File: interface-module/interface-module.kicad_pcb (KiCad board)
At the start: 2 copper layers, 79 x 83 mm, 117 parts, among them J1 Conn_01x08, J2 Conn_01x08, J3 Conn_01x02, Q201 PMOS, Q202 NMOS, Q203 PMOS, Q204 NMOS, Q205 PMOS, Q206 NMOS, Q207 PMOS, Q208 NMOS, Q209 PMOS, Q210 NMOS, Q211 PMOS, Q212 NMOS, Q213 PMOS, Q214 NMOS, Q215 PMOS, Q216 NMOS, SW1 SW_Coded_SH-7050, U101 MCP3464, U201 140357145200, U202 140357145200, U203 140357145200, U204 140357145200, U205 140357145200, U206 140357145200, U207 140357145200, U208 140357145200, U301 TCA9548

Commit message: Added address pin labels
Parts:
- R2: value CFG1 -> INFO1
- R4: value CFG2 -> INFO2
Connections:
- net Net-(U1-PA4) renamed /ADDR_4
- net Net-(U1-PA5) renamed /ADDR_1
- net Net-(U1-PA6) renamed /ADDR_8
- net Net-(U1-PA7) renamed /ADDR_2

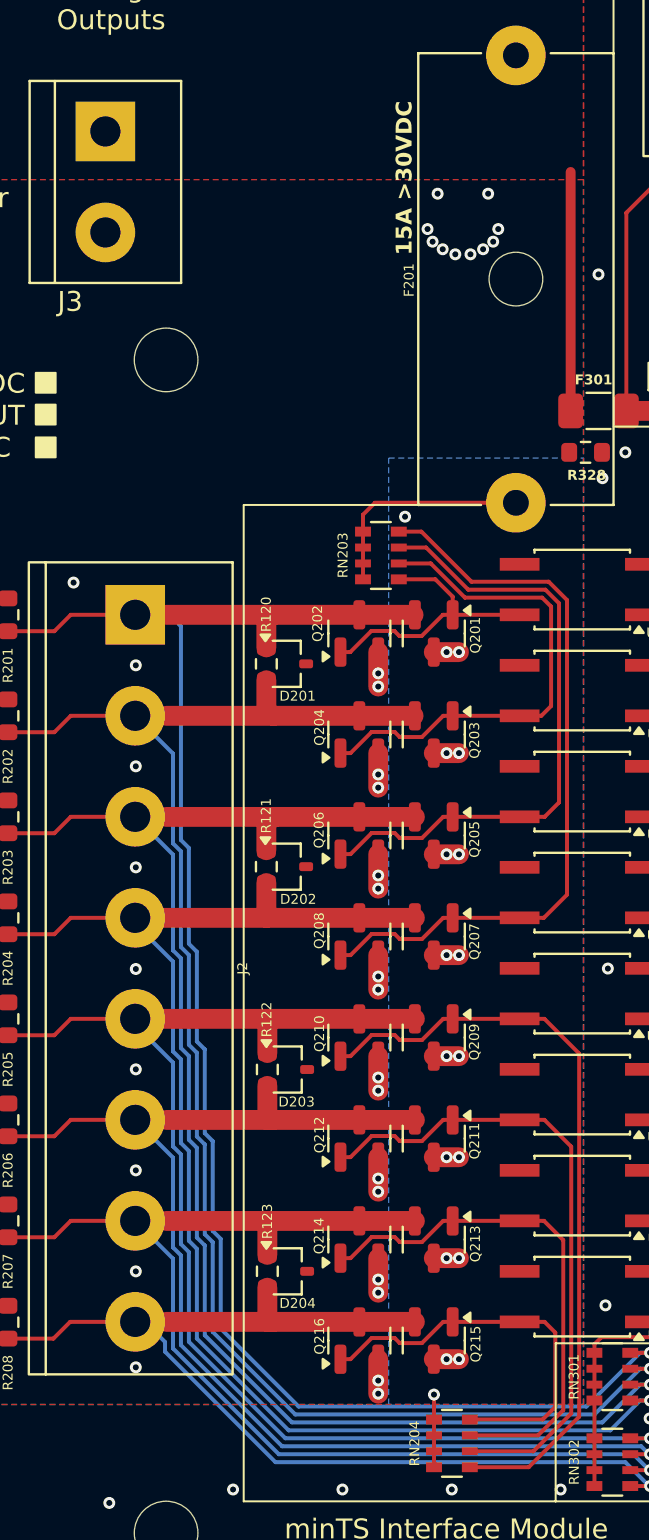
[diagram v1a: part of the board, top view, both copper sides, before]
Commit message: Revision, updated diodes and transistors
Moved to a more robust transistor arrangement with a new zener diode
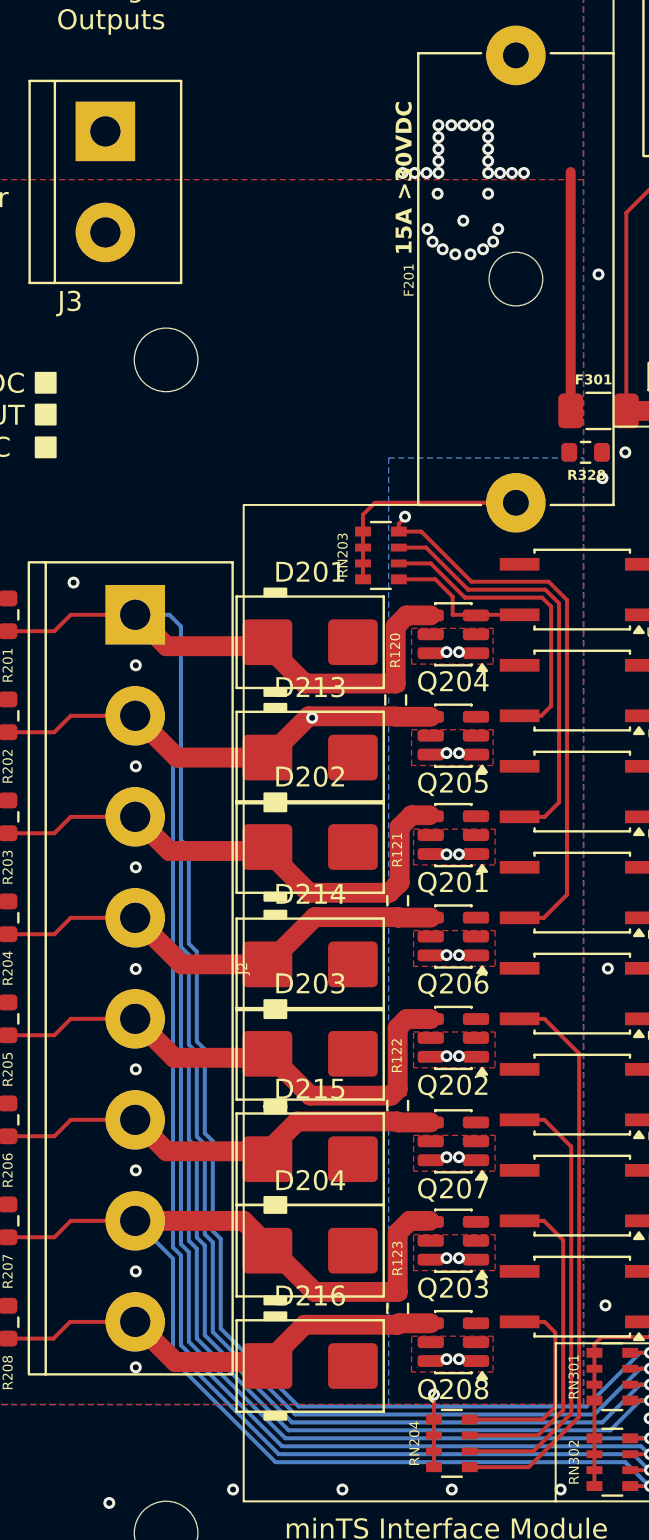
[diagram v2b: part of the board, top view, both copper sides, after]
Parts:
- removed Q209, Q211, Q213, Q215: PMOS, Package_TO_SOT_SMD:SOT-23
- removed Q210, Q212, Q214, Q216: NMOS, Package_TO_SOT_SMD:SOT-23
- added D213: SMBJ5.0A, PCM_Diode_SMD_AKL:D_SMB, F.Cu at (121.8, 103.7)
- added D214: SMBJ5.0A, PCM_Diode_SMD_AKL:D_SMB, F.Cu at (121.8, 114.1)
- added D215: SMBJ5.0A, PCM_Diode_SMD_AKL:D_SMB, F.Cu at (121.8, 123.9)
- added D216: SMBJ5.0A, PCM_Diode_SMD_AKL:D_SMB, F.Cu at (121.8, 134.3)
- D201, D202, D203, D204: value MMBD717LT1G -> SMBJ5.0A; footprint Package_TO_SOT_SMD:SOT-323_SC-70 -> PCM_Diode_SMD_AKL:D_SMB
- Q201, Q203, Q205, Q207: value PMOS -> DMP3050LVT-7; footprint Package_TO_SOT_SMD:SOT-23 -> Package_TO_SOT_SMD:TSOT-23-6
- Q202, Q204, Q206, Q208: value NMOS -> DMP3050LVT-7; footprint Package_TO_SOT_SMD:SOT-23 -> Package_TO_SOT_SMD:TSOT-23-6
- moved Q203 25.5 mm to (129.0, 128.0), turned to 180 degrees
- moved Q208 20.9 mm to (129.0, 133.1), turned to 180 degrees
- moved Q202 20.9 mm to (129.0, 117.8), turned to 180 degrees
- moved Q207 10.3 mm to (129.0, 123.0), turned to 180 degrees
- moved Q201 10.2 mm to (129.0, 107.6), turned to 180 degrees
- moved Q206 6.94 mm to (129.0, 112.7), turned to 180 degrees
- moved Q204 6.91 mm to (129.0, 97.5), turned to 180 degrees
- moved R121 6.82 mm to (126.2, 110.9)
- moved R123 6.81 mm to (126.2, 131.4)
- moved R122 6.80 mm to (126.2, 121.2)
- moved R120 6.75 mm to (126.1, 100.8)
- moved Q205 5.12 mm to (129.0, 102.6), turned to 180 degrees
- moved D201 1.62 mm to (121.8, 97.9)
- moved D202 1.56 mm to (121.8, 108.2)
- moved D204 1.55 mm to (121.8, 128.5)
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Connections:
- D201 pad 2: OUT1/IN0- -> AUX_POW-
- D202 pad 2: OUT3/IN1- -> AUX_POW-
- D203 pad 2: OUT5/IN2- -> AUX_POW-
- D204 pad 2: OUT7/IN3- -> AUX_POW-
- Q201 pad 1: /outputs/~{ISO_OUT_0} -> VPOW
- Q201 pad 2: OUT0/IN0+ -> VPOW
- Q201 pad 3: VPOW -> AUX_POW-
- Q202 pad 1: /outputs/~{ISO_OUT_0} -> VPOW
- Q202 pad 2: AUX_POW- -> VPOW
- Q202 pad 3: OUT0/IN0+ -> AUX_POW-
- Q203 pad 1: /outputs/~{ISO_OUT_1} -> VPOW
- Q203 pad 2: OUT1/IN0- -> VPOW
- Q203 pad 3: VPOW -> AUX_POW-
- Q204 pad 1: /outputs/~{ISO_OUT_1} -> VPOW
- Q204 pad 2: AUX_POW- -> VPOW
- Q204 pad 3: OUT1/IN0- -> AUX_POW-
- Q205 pad 1: /outputs/~{ISO_OUT_2} -> VPOW
- Q205 pad 2: OUT2/IN1+ -> VPOW
- Q205 pad 3: VPOW -> AUX_POW-
- Q206 pad 1: /outputs/~{ISO_OUT_2} -> VPOW
- Q206 pad 2: AUX_POW- -> VPOW
- Q206 pad 3: OUT2/IN1+ -> AUX_POW-
- Q207 pad 1: /outputs/~{ISO_OUT_3} -> VPOW
- Q207 pad 2: OUT3/IN1- -> VPOW
- Q207 pad 3: VPOW -> AUX_POW-
- Q208 pad 1: /outputs/~{ISO_OUT_3} -> VPOW
- Q208 pad 2: AUX_POW- -> VPOW
- Q208 pad 3: OUT3/IN1- -> AUX_POW-
- RN203 pad 5: /outputs/~{ISO_OUT_0} -> AUX_POW-
- RN203 pad 6: /outputs/~{ISO_OUT_1} -> AUX_POW-
- RN203 pad 7: /outputs/~{ISO_OUT_2} -> AUX_POW-
- RN203 pad 8: /outputs/~{ISO_OUT_3} -> AUX_POW-
- RN204 pad 5: /outputs/~{ISO_OUT_4} -> AUX_POW-
- RN204 pad 6: /outputs/~{ISO_OUT_5} -> AUX_POW-
- RN204 pad 7: /outputs/~{ISO_OUT_6} -> AUX_POW-
- RN204 pad 8: /outputs/~{ISO_OUT_7} -> AUX_POW-
- U201 pad 4: /outputs/~{ISO_OUT_0} -> AUX_POW-
- U202 pad 4: /outputs/~{ISO_OUT_1} -> AUX_POW-
- U203 pad 4: /outputs/~{ISO_OUT_2} -> AUX_POW-
- U204 pad 4: /outputs/~{ISO_OUT_3} -> AUX_POW-
- U205 pad 4: /outputs/~{ISO_OUT_4} -> AUX_POW-
- U206 pad 4: /outputs/~{ISO_OUT_5} -> AUX_POW-
- U207 pad 4: /outputs/~{ISO_OUT_6} -> AUX_POW-
- U208 pad 4: /outputs/~{ISO_OUT_7} -> AUX_POW-
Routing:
- net AUX_POW-: track 13.9 -> 150.1 mm, vias 36 -> 21
- net /outputs/~{ISO_OUT_4}: track 38.5 -> 0.00 mm
- net /outputs/~{ISO_OUT_3}: track 37.6 -> 0.00 mm
- net /outputs/~{ISO_OUT_5}: track 32.5 -> 0.00 mm
- net /outputs/~{ISO_OUT_2}: track 31.5 -> 0.00 mm
- net /outputs/~{ISO_OUT_6}: track 26.4 -> 0.00 mm
- net /outputs/~{ISO_OUT_1}: track 25.3 -> 0.00 mm
- net /outputs/~{ISO_OUT_7}: track 20.3 -> 0.00 mm
- net /outputs/~{ISO_OUT_0}: track 13.7 -> 0.00 mm
- net VPOW: track 25.0 -> 14.9 mm
- net OUT2/IN1+: track 118.6 -> 124.1 mm
- net OUT6/IN3+: track 87.6 -> 92.9 mm
- net OUT0/IN0+: track 136.0 -> 141.3 mm
- net OUT4/IN2+: track 103.5 -> 107.6 mm
- net OUT1/IN0-: track 129.0 -> 131.4 mm, vias 2 -> 3
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- added copper zone on F.Cu, net VPOW

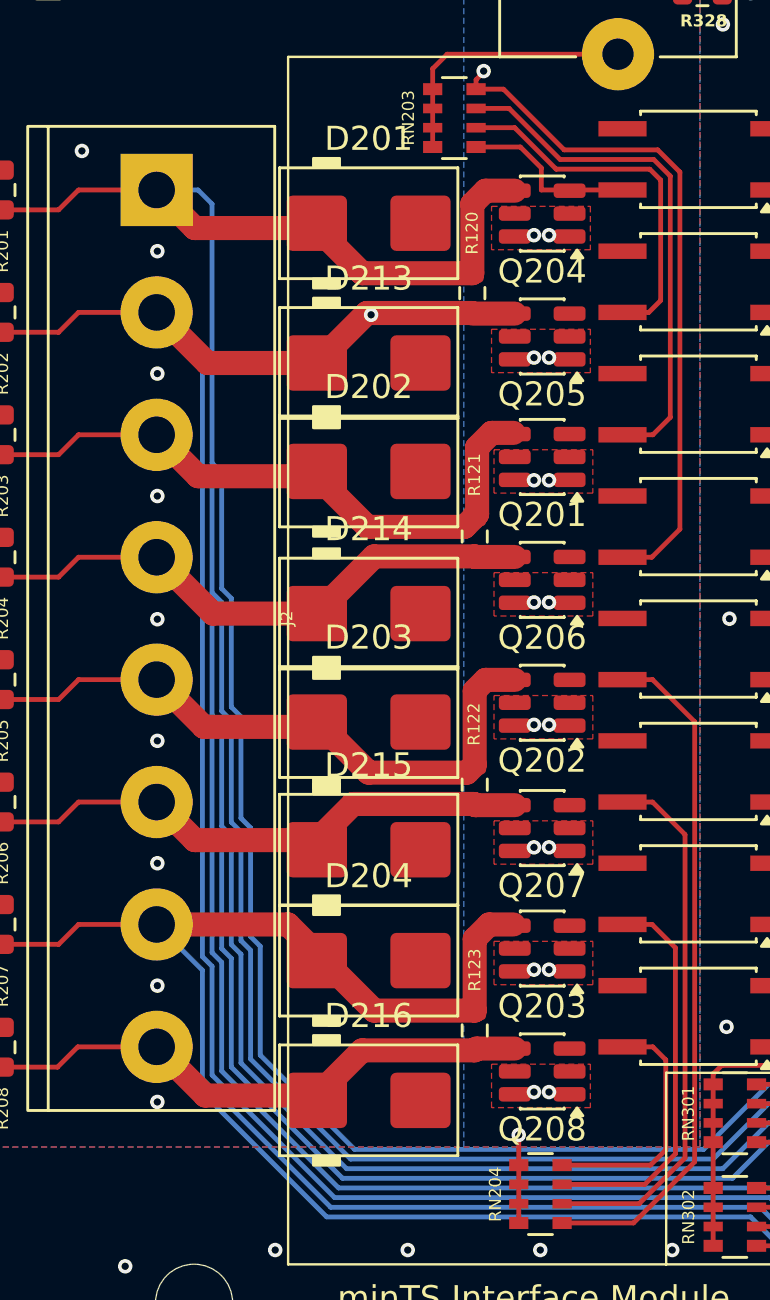
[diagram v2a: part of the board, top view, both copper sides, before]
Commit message: Fixed transistor tracing
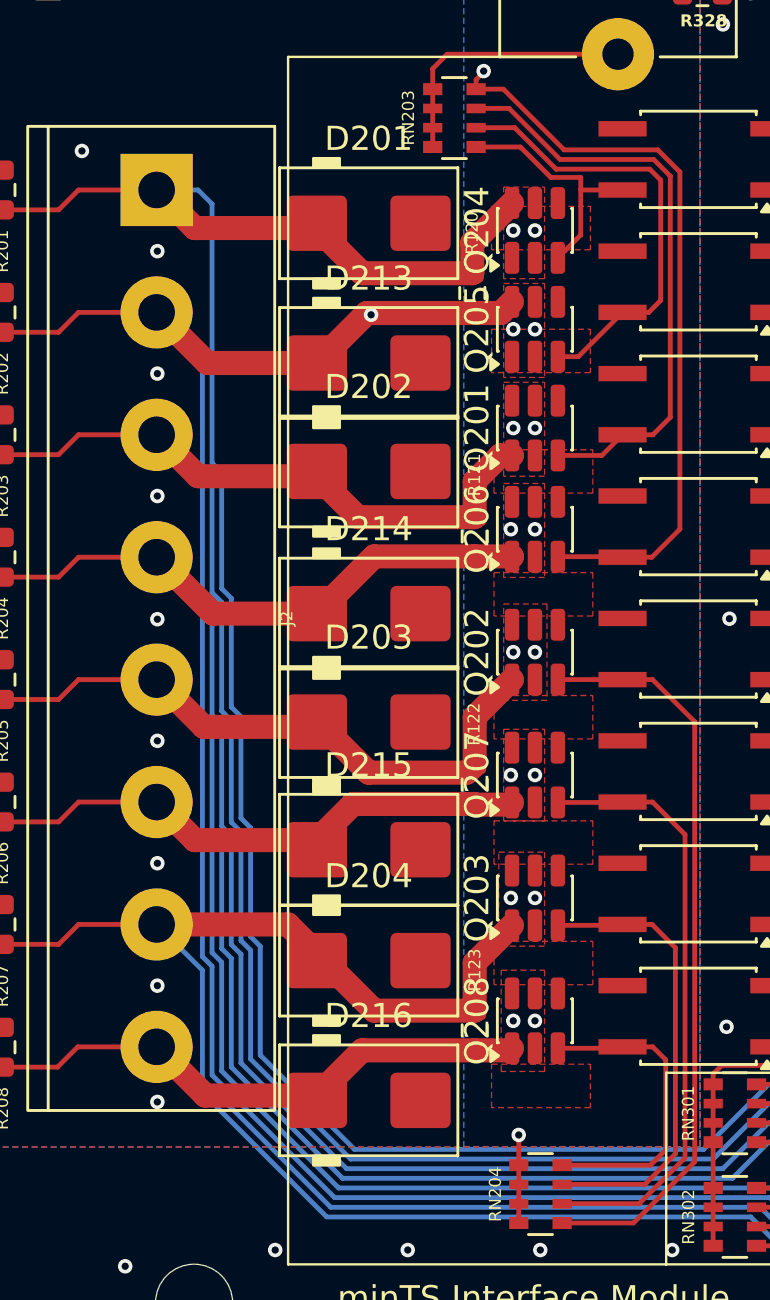
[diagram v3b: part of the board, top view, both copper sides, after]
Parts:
- moved Q207 2.22 mm to (128.7, 120.8), turned to 90 degrees
- moved Q206 2.12 mm to (128.7, 110.6), turned to 90 degrees
- moved Q202 2.12 mm to (128.7, 115.7), turned to 90 degrees
- moved Q203 2.12 mm to (128.7, 125.9), turned to 90 degrees
- moved Q208 2.12 mm to (128.7, 131.0), turned to 90 degrees
- moved Q201 1.24 mm to (128.7, 106.4), turned to 90 degrees
- moved Q204 0.76 mm to (128.7, 98.2), turned to 90 degrees
- moved Q205 0.42 mm to (128.7, 102.3), turned to 90 degrees
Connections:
- Q201 pad 1: VPOW -> OUT2/IN1+
- Q201 pad 2: VPOW -> OUT2/IN1+
- Q201 pad 3: AUX_POW- -> /outputs/~{ISO_OUT_2}
- Q201 pad 4: OUT2/IN1+ -> VPOW
- Q201 pad 5: VPOW -> OUT2/IN1+
- Q201 pad 6: VPOW -> OUT2/IN1+
- Q202 pad 1: VPOW -> OUT4/IN2+
- Q202 pad 2: VPOW -> OUT4/IN2+
- Q202 pad 3: AUX_POW- -> /outputs/~{ISO_OUT_4}
- Q202 pad 4: OUT4/IN2+ -> VPOW
- Q202 pad 5: VPOW -> OUT4/IN2+
- Q202 pad 6: VPOW -> OUT4/IN2+
- Q203 pad 1: VPOW -> OUT6/IN3+
- Q203 pad 2: VPOW -> OUT6/IN3+
- Q203 pad 3: AUX_POW- -> /outputs/~{ISO_OUT_6}
- Q203 pad 4: OUT6/IN3+ -> VPOW
- Q203 pad 5: VPOW -> OUT6/IN3+
- Q203 pad 6: VPOW -> OUT6/IN3+
- Q204 pad 1: VPOW -> OUT0/IN0+
- Q204 pad 2: VPOW -> OUT0/IN0+
- Q204 pad 3: AUX_POW- -> /outputs/~{ISO_OUT_0}
- Q204 pad 4: OUT0/IN0+ -> VPOW
- Q204 pad 5: VPOW -> OUT0/IN0+
- Q204 pad 6: VPOW -> OUT0/IN0+
- Q205 pad 1: VPOW -> OUT1/IN0-
- Q205 pad 2: VPOW -> OUT1/IN0-
- Q205 pad 3: AUX_POW- -> /outputs/~{ISO_OUT_1}
- Q205 pad 4: OUT1/IN0- -> VPOW
- Q205 pad 5: VPOW -> OUT1/IN0-
- Q205 pad 6: VPOW -> OUT1/IN0-
- Q206 pad 1: VPOW -> OUT3/IN1-
- Q206 pad 2: VPOW -> OUT3/IN1-
- Q206 pad 3: AUX_POW- -> /outputs/~{ISO_OUT_3}
- Q206 pad 4: OUT3/IN1- -> VPOW
- Q206 pad 5: VPOW -> OUT3/IN1-
- Q206 pad 6: VPOW -> OUT3/IN1-
- Q207 pad 1: VPOW -> OUT5/IN2-
- Q207 pad 2: VPOW -> OUT5/IN2-
- Q207 pad 3: AUX_POW- -> /outputs/~{ISO_OUT_5}
- Q207 pad 4: OUT5/IN2- -> VPOW
- Q207 pad 5: VPOW -> OUT5/IN2-
- Q207 pad 6: VPOW -> OUT5/IN2-
- Q208 pad 1: VPOW -> OUT7/IN3-
- Q208 pad 2: VPOW -> OUT7/IN3-
- Q208 pad 3: AUX_POW- -> /outputs/~{ISO_OUT_7}
- Q208 pad 4: OUT7/IN3- -> VPOW
- Q208 pad 5: VPOW -> OUT7/IN3-
- Q208 pad 6: VPOW -> OUT7/IN3-
- RN203 pad 5: AUX_POW- -> /outputs/~{ISO_OUT_0}
- RN203 pad 6: AUX_POW- -> /outputs/~{ISO_OUT_1}
- RN203 pad 7: AUX_POW- -> /outputs/~{ISO_OUT_2}
- RN203 pad 8: AUX_POW- -> /outputs/~{ISO_OUT_3}
- RN204 pad 5: AUX_POW- -> /outputs/~{ISO_OUT_4}
- RN204 pad 6: AUX_POW- -> /outputs/~{ISO_OUT_5}
- RN204 pad 7: AUX_POW- -> /outputs/~{ISO_OUT_6}
- RN204 pad 8: AUX_POW- -> /outputs/~{ISO_OUT_7}
- U201 pad 4: AUX_POW- -> /outputs/~{ISO_OUT_0}
- U202 pad 4: AUX_POW- -> /outputs/~{ISO_OUT_1}
- U203 pad 4: AUX_POW- -> /outputs/~{ISO_OUT_2}
- U204 pad 4: AUX_POW- -> /outputs/~{ISO_OUT_3}
- U205 pad 4: AUX_POW- -> /outputs/~{ISO_OUT_4}
- U206 pad 4: AUX_POW- -> /outputs/~{ISO_OUT_5}
- U207 pad 4: AUX_POW- -> /outputs/~{ISO_OUT_6}
- U208 pad 4: AUX_POW- -> /outputs/~{ISO_OUT_7}
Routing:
- net AUX_POW-: track 150.1 -> 0.00 mm
- net /outputs/~{ISO_OUT_4}: track 0.00 -> 31.2 mm
- net /outputs/~{ISO_OUT_3}: track 0.00 -> 31.1 mm
- net /outputs/~{ISO_OUT_5}: track 0.00 -> 25.1 mm
- net /outputs/~{ISO_OUT_2}: track 0.00 -> 24.6 mm
- net /outputs/~{ISO_OUT_6}: track 0.00 -> 19.1 mm
- net /outputs/~{ISO_OUT_1}: track 0.00 -> 18.8 mm
- net /outputs/~{ISO_OUT_7}: track 0.00 -> 13.0 mm
- net /outputs/~{ISO_OUT_0}: track 0.00 -> 10.3 mm
- net OUT2/IN1+: track 124.1 -> 122.5 mm, vias 2 -> 4
- net OUT0/IN0+: track 141.3 -> 140.1 mm, vias 2 -> 4
- net OUT4/IN2+: track 107.6 -> 106.9 mm, vias 2 -> 4
- net OUT6/IN3+: track 92.9 -> 92.3 mm, vias 2 -> 4
- net OUT7/IN3-: track 85.0 -> 84.9 mm, vias 2 -> 4
- net OUT3/IN1-: track 115.0 -> 114.9 mm, vias 2 -> 4
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- added copper zone on F.Cu, net OUT0/IN0+
- added copper zone on F.Cu, net OUT1/IN0-
- added copper zone on F.Cu, net OUT2/IN1+
- added copper zone on F.Cu, net OUT3/IN1-
- added copper zone on F.Cu, net OUT4/IN2+
- added copper zone on F.Cu, net OUT5/IN2-
- added copper zone on F.Cu, net OUT6/IN3+
- added copper zone on F.Cu, net OUT7/IN3-

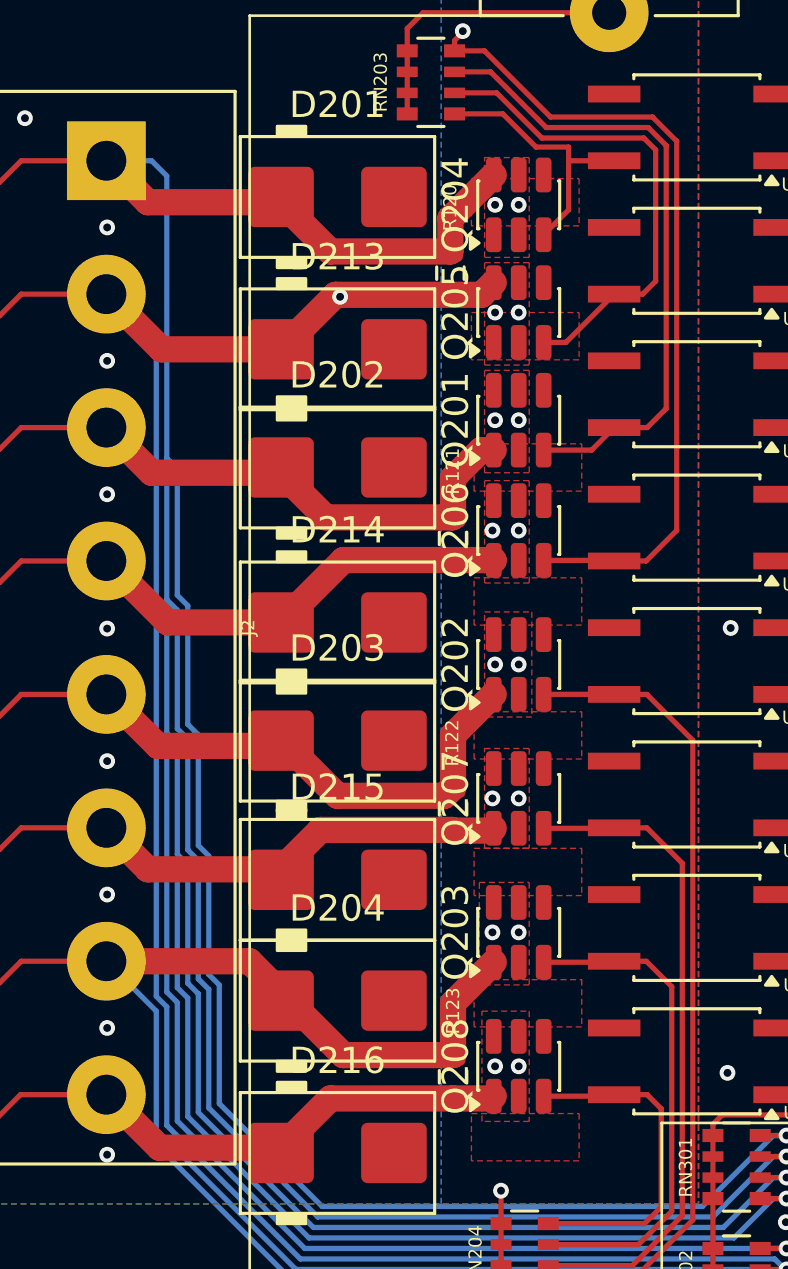
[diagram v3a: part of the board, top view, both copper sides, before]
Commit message: Updated with better traces
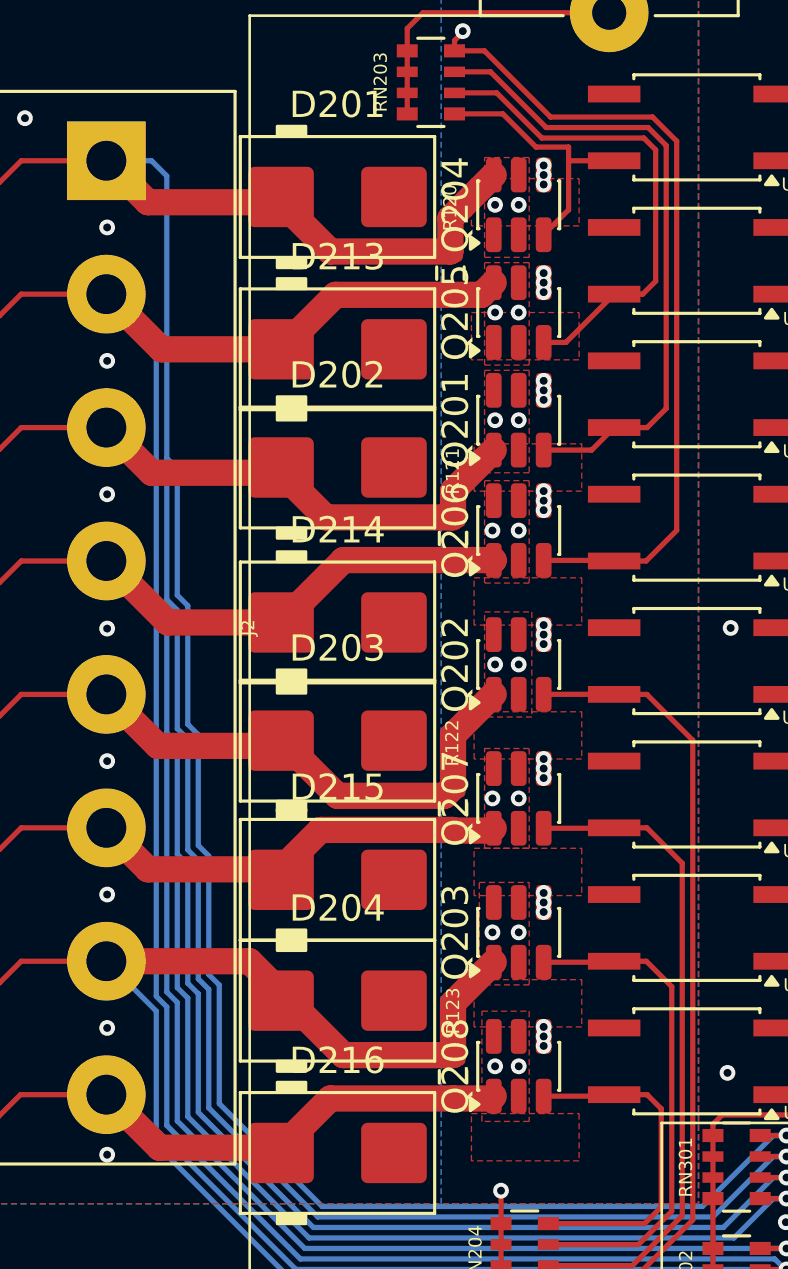
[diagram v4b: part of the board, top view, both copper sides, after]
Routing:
- net VPOW: vias 1 -> 25
- net OUT1/IN0-: vias 5 -> 4
